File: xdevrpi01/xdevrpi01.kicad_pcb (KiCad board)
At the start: 4 copper layers, 50.8 x 22.9 mm, 39 parts, among them P1 USB_C_Plug_USB2.0, SW1 BOOT, SW2 RST, U1 AP2112K-3.3, U2 RP2040, U3 W25Q128JVS, U4 Feather, Y1 12MHz

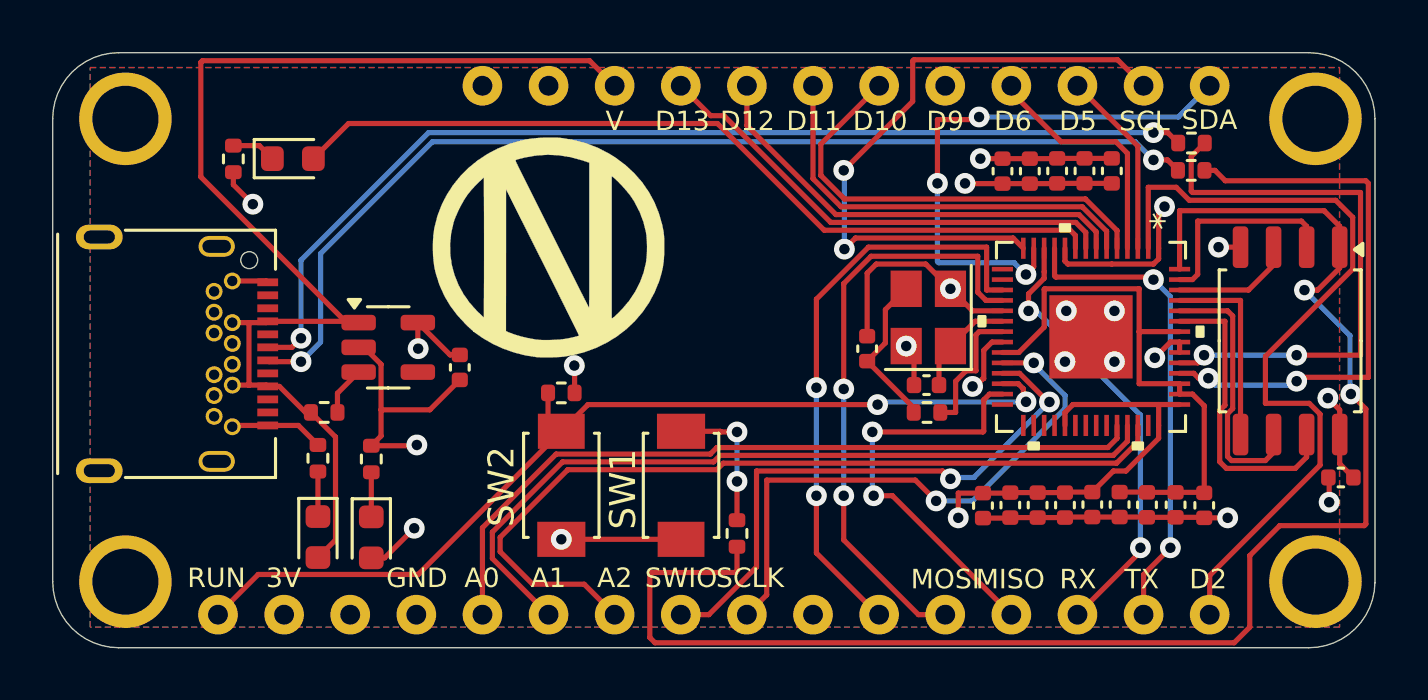
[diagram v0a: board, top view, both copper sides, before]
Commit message: fix regulator pin
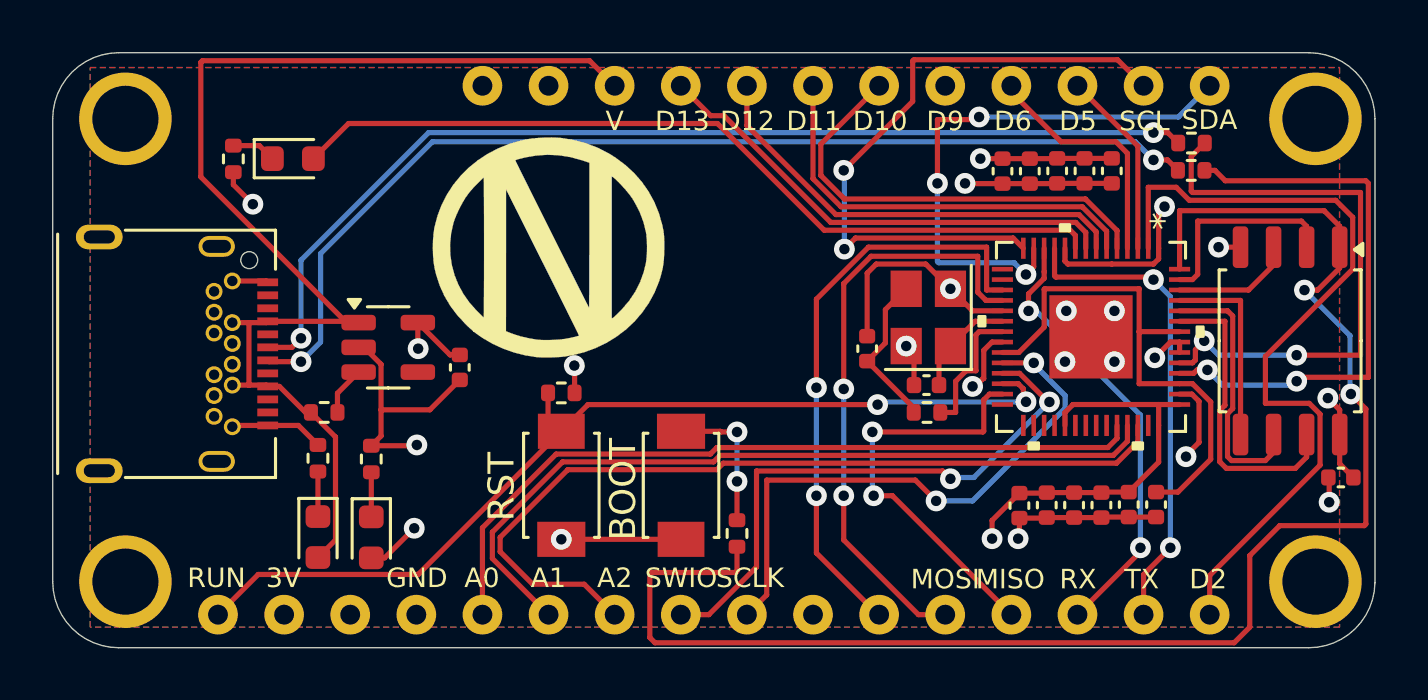
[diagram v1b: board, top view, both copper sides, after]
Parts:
- removed C4, C5: 100nF, Capacitor_SMD:C_0402_1005Metric
- removed C6: 1uF, Capacitor_SMD:C_0402_1005Metric
- moved C13 1.40 mm to (161.9, 105.8)
- moved C14 1.40 mm to (164.0, 105.8)
- moved C15 1.40 mm to (160.8, 105.8)
- moved C17 1.40 mm to (166.1, 105.8)
- moved C18 1.40 mm to (165.1, 105.8)
- moved C12 1.40 mm to (162.9, 105.8)
- renumbered SW1 to BOOT, SW2 to RST
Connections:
- U2 pad 44: +1V1 -> +3V3
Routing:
- net GND: track 47.5 -> 44.2 mm
- net +3V3: track 42.0 -> 44.7 mm, vias 9 -> 10
- net +1V1: track 22.0 -> 20.2 mm
- net Net-(U2-USB_DP): track 22.0 -> 22.6 mm

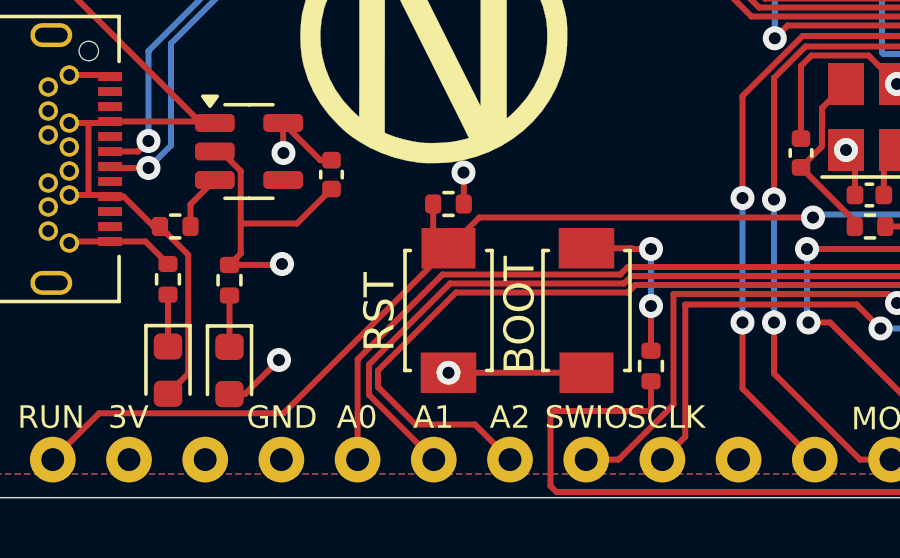
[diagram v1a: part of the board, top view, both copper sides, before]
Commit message: adjust switch text
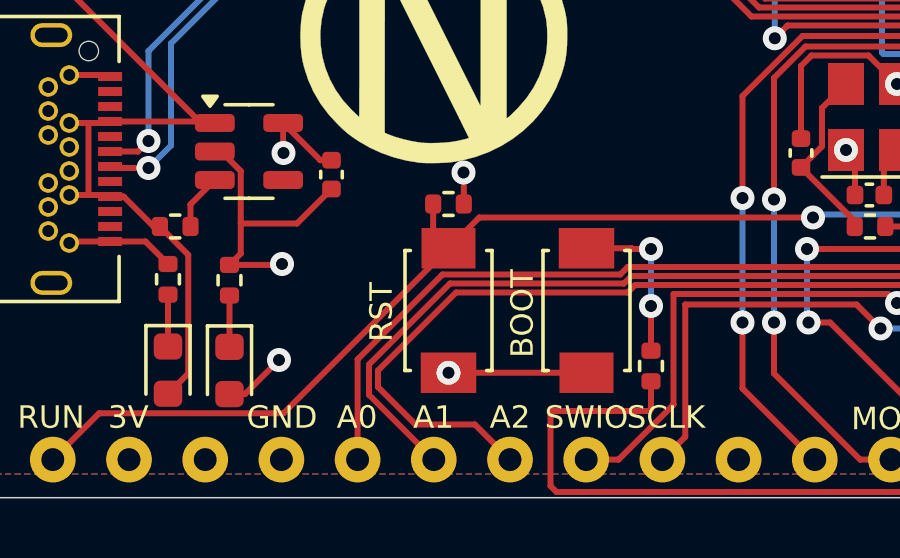
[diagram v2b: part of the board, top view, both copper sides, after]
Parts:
- renumbered BOOT to SW1, RST to SW2
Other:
- board text added: "BOOT"
- board text added: "RST"
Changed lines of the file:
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@@
 		(at 143.25 105.05 -90)
 		(descr "LCSC-C720477 ")
-		(property "Reference" "RST"
+		(property "Reference" "SW2"
 			(at 0.05 2.3 90)
 			(unlocked yes)
-			(layer "F.SilkS")
+			(layer "F.Fab")
 			(effects
 				(font
@@
 		(at 147.85 105.05 90)
 		(descr "LCSC-C720477 ")
-		(property "Reference" "BOOT"
+		(property "Reference" "SW1"
 			(at -0.15 -2.23 90)
 			(unlocked yes)
-			(layer "F.SilkS")
+			(layer "F.Fab")
 			(effects
 				(font
@@
 		)
 	)
+	(gr_text "BOOT"
+		(at 146.15 105.15 90)
+		(layer "F.SilkS")
+		(effects
+			(font
+				(size 0.75 0.75)
+				(thickness 0.1)
+			)
+			(justify bottom)
+		)
+	)
 	(gr_text "GND"
 		(at 137.7 109.05 0)
@@
 		(layer "F.SilkS")
 		(effects
+			(font
+				(size 0.75 0.75)
+				(thickness 0.1)
+			)
+			(justify bottom)
+		)
+	)
+	(gr_text "RST"
+		(at 141.45 105.1 90)
+		(layer "F.SilkS")
+		(effects
